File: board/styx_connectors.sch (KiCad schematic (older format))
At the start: 15 parts, among them J3 Conn_01x08, J4 Styx_P4, J5 Styx_P5

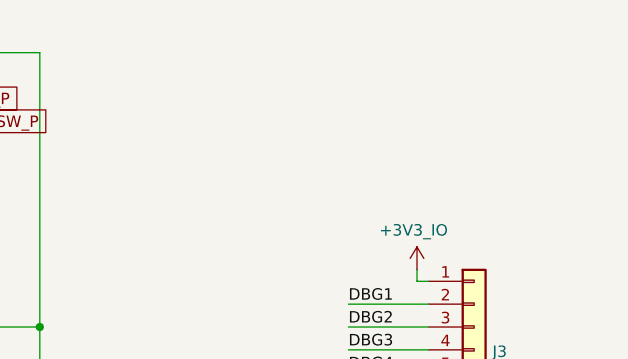
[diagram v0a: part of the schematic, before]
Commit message: Board: initial rearranging to allow for a cover
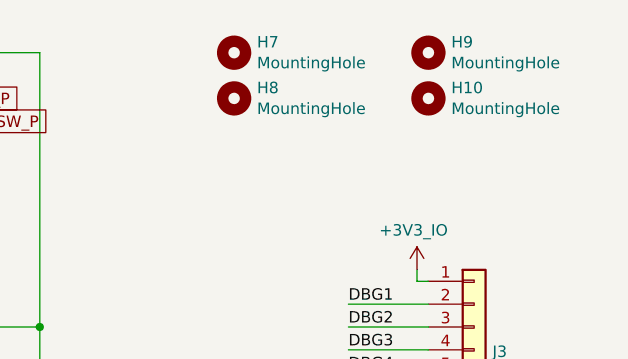
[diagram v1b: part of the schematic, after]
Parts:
- added H10, H7, H8, H9: MountingHole, agc_monitor:MountingHole_ANSI_4, symbol Mechanical:MountingHole
- J3: footprint Connector_PinSocket_2.54mm:PinSocket_2x04_P2.54mm_Vertical -> Connector_PinSocket_2.54mm:PinSocket_2x04_P2.54mm_Horizontal
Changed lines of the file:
@@
 F 0 "J3" H 9830 2142 50  0000 L CNN
 F 1 "Conn_01x08" H 9830 2051 50  0000 L CNN
-F 2 "Connector_PinSocket_2.54mm:PinSocket_2x04_P2.54mm_Vertical" H 9750 2150 50  0001 C CNN
+F 2 "Connector_PinSocket_2.54mm:PinSocket_2x04_P2.54mm_Horizontal" H 9750 2150 50  0001 C CNN
 F 3 "~" H 9750 2150 50  0001 C CNN
 	1    9750 2150
@@
 	4750 6150 4750 6100
 Connection ~ 4750 6100
+$Comp
+L Mechanical:MountingHole H7
+U 1 1 5C9779E4
+P 8700 850
+F 0 "H7" H 8800 896 50  0000 L CNN
+F 1 "MountingHole" H 8800 805 50  0000 L CNN
+F 2 "agc_monitor:MountingHole_ANSI_4" H 8700 850 50  0001 C CNN
+F 3 "~" H 8700 850 50  0001 C CNN
+	1    8700 850
+	1    0    0    -1
+$EndComp
+$Comp
+L Mechanical:MountingHole H8
+U 1 1 5C98D89C
+P 8700 1050
+F 0 "H8" H 8800 1096 50  0000 L CNN
+F 1 "MountingHole" H 8800 1005 50  0000 L CNN
+F 2 "agc_monitor:MountingHole_ANSI_4" H 8700 1050 50  0001 C CNN
+F 3 "~" H 8700 1050 50  0001 C CNN
+	1    8700 1050
+	1    0    0    -1
+$EndComp
+$Comp
+L Mechanical:MountingHole H9
+U 1 1 5C9A3644
+P 9550 850
+F 0 "H9" H 9650 896 50  0000 L CNN
+F 1 "MountingHole" H 9650 805 50  0000 L CNN
+F 2 "agc_monitor:MountingHole_ANSI_4" H 9550 850 50  0001 C CNN
+F 3 "~" H 9550 850 50  0001 C CNN
+	1    9550 850
+	1    0    0    -1
+$EndComp
+$Comp
+L Mechanical:MountingHole H10
+U 1 1 5C9A364A
+P 9550 1050
+F 0 "H10" H 9650 1096 50  0000 L CNN
+F 1 "MountingHole" H 9650 1005 50  0000 L CNN
+F 2 "agc_monitor:MountingHole_ANSI_4" H 9550 1050 50  0001 C CNN
+F 3 "~" H 9550 1050 50  0001 C CNN
+	1    9550 1050
+	1    0    0    -1
+$EndComp
 $EndSCHEMATC

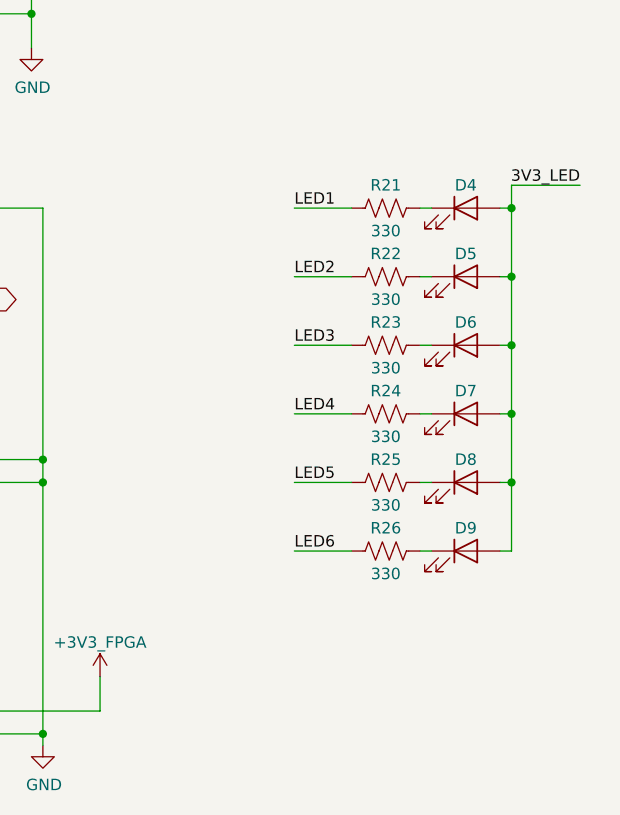
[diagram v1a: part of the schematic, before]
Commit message: Board: more rearranging work on the front; a bit more yet to come
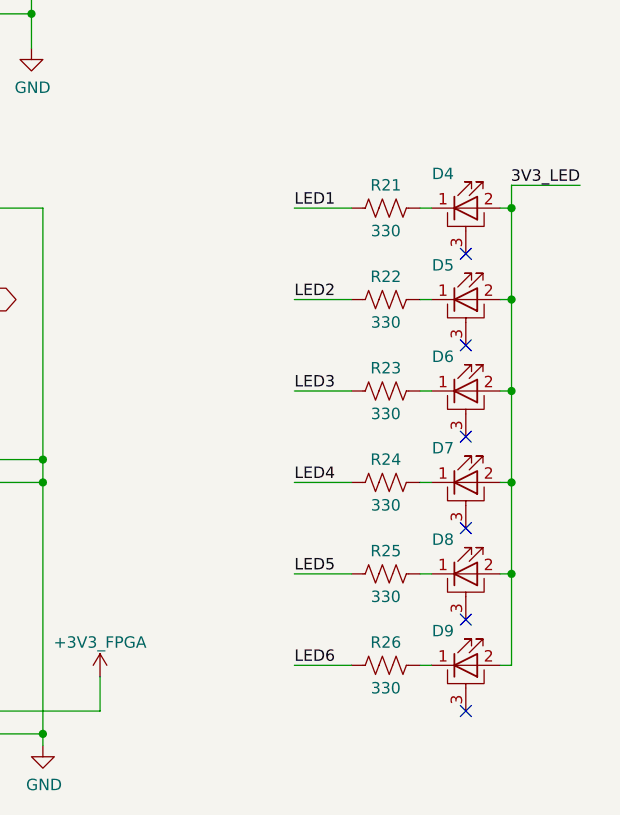
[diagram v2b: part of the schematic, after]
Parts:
- removed D4, D5, D6, D7, D8, D9: LED, LED_SMD:LED_0603_1608Metric, symbol Device:LED
- added D4, D5, D6, D7, D8, D9: LED_PAD, agc_monitor:apa3010, symbol Device:LED_PAD
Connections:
- net 3V3_LED: now also D4.2 (A), D5.2 (A), D6.2 (A), D7.2 (A), D8.2 (A), D9.2 (A)
- net at R25.1: now also D8.1 (K)
- net at R26.1: now also D9.1 (K)
- net at R21.1: now also D4.1 (K)
- net at R22.1: now also D5.1 (K)
- net at R23.1: now also D6.1 (K)
- net at R24.1: now also D7.1 (K)
- no-connect marks 16 -> 22
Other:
- moved on the sheet: R22, R23, R24, R25, R26
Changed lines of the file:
@@
 Text Label 9200 2250 0    50   ~ 0
 DBG4
-$Comp
-L Device:LED D4
-U 1 1 5E9D86D0
-P 9750 3900
-F 0 "D4" H 9750 4000 50  0000 C CNN
-F 1 "LED" H 9741 4025 50  0001 C CNN
-F 2 "LED_SMD:LED_0603_1608Metric" H 9750 3900 50  0001 C CNN
-F 3 "~" H 9750 3900 50  0001 C CNN
-	1    9750 3900
-	1    0    0    -1
-$EndComp
 Wire Wire Line
 	9250 3900 9000 3900
@@
 Wire Wire Line
 	9950 3900 9950 3800
-$Comp
-L Device:LED D5
-U 1 1 5EA444DA
-P 9750 4200
-F 0 "D5" H 9750 4300 50  0000 C CNN
-F 1 "LED" H 9741 4325 50  0001 C CNN
-F 2 "LED_SMD:LED_0603_1608Metric" H 9750 4200 50  0001 C CNN
-F 3 "~" H 9750 4200 50  0001 C CNN
-	1    9750 4200
-	1    0    0    -1
-$EndComp
-Wire Wire Line
-	9250 4200 9000 4200
-Text Label 9000 4200 0    50   ~ 0
+Wire Wire Line
+	9250 4300 9000 4300
+Text Label 9000 4300 0    50   ~ 0
 LED2
 $Comp
 L Device:R_US R22
 U 1 1 5EA444E2
-P 9400 4200
-F 0 "R22" V 9300 4200 50  0000 C CNN
-F 1 "330" V 9500 4200 50  0000 C CNN
-F 2 "Resistor_SMD:R_0603_1608Metric" V 9440 4190 50  0001 C CNN
-F 3 "~" H 9400 4200 50  0001 C CNN
-	1    9400 4200
-	0    1    1    0
-$EndComp
-Wire Wire Line
-	9600 4200 9550 4200
-Wire Wire Line
-	9950 3900 9950 4200
-Wire Wire Line
-	9950 4200 9900 4200
+P 9400 4300
+F 0 "R22" V 9300 4300 50  0000 C CNN
+F 1 "330" V 9500 4300 50  0000 C CNN
+F 2 "Resistor_SMD:R_0603_1608Metric" V 9440 4290 50  0001 C CNN
+F 3 "~" H 9400 4300 50  0001 C CNN
+	1    9400 4300
+	0    1    1    0
+$EndComp
+Wire Wire Line
+	9600 4300 9550 4300
+Wire Wire Line
+	9950 3900 9950 4300
+Wire Wire Line
+	9950 4300 9900 4300
 Connection ~ 9950 3900
-$Comp
-L Device:LED D6
-U 1 1 5EA8C97F
-P 9750 4500
-F 0 "D6" H 9750 4600 50  0000 C CNN
-F 1 "LED" H 9741 4625 50  0001 C CNN
-F 2 "LED_SMD:LED_0603_1608Metric" H 9750 4500 50  0001 C CNN
-F 3 "~" H 9750 4500 50  0001 C CNN
-	1    9750 4500
-	1    0    0    -1
-$EndComp
-Wire Wire Line
-	9250 4500 9000 4500
-Text Label 9000 4500 0    50   ~ 0
+Wire Wire Line
+	9250 4700 9000 4700
+Text Label 9000 4700 0    50   ~ 0
 LED3
 $Comp
 L Device:R_US R23
 U 1 1 5EA8C987
-P 9400 4500
-F 0 "R23" V 9300 4500 50  0000 C CNN
-F 1 "330" V 9500 4500 50  0000 C CNN
-F 2 "Resistor_SMD:R_0603_1608Metric" V 9440 4490 50  0001 C CNN
-F 3 "~" H 9400 4500 50  0001 C CNN
-	1    9400 4500
-	0    1    1    0
-$EndComp
-Wire Wire Line
-	9600 4500 9550 4500
-Wire Wire Line
-	9900 4500 9950 4500
-$Comp
-L Device:LED D7
-U 1 1 5EA8C98F
-P 9750 4800
-F 0 "D7" H 9750 4900 50  0000 C CNN
-F 1 "LED" H 9741 4925 50  0001 C CNN
-F 2 "LED_SMD:LED_0603_1608Metric" H 9750 4800 50  0001 C CNN
-F 3 "~" H 9750 4800 50  0001 C CNN
-	1    9750 4800
-	1    0    0    -1
-$EndComp
-Wire Wire Line
-	9250 4800 9000 4800
-Text Label 9000 4800 0    50   ~ 0
+P 9400 4700
+F 0 "R23" V 9300 4700 50  0000 C CNN
+F 1 "330" V 9500 4700 50  0000 C CNN
+F 2 "Resistor_SMD:R_0603_1608Metric" V 9440 4690 50  0001 C CNN
+F 3 "~" H 9400 4700 50  0001 C CNN
+	1    9400 4700
+	0    1    1    0
+$EndComp
+Wire Wire Line
+	9600 4700 9550 4700
+Wire Wire Line
+	9900 4700 9950 4700
+Wire Wire Line
+	9250 5100 9000 5100
+Text Label 9000 5100 0    50   ~ 0
 LED4
 $Comp
 L Device:R_US R24
 U 1 1 5EA8C997
-P 9400 4800
-F 0 "R24" V 9300 4800 50  0000 C CNN
-F 1 "330" V 9500 4800 50  0000 C CNN
-F 2 "Resistor_SMD:R_0603_1608Metric" V 9440 4790 50  0001 C CNN
-F 3 "~" H 9400 4800 50  0001 C CNN
-	1    9400 4800
-	0    1    1    0
-$EndComp
-Wire Wire Line
-	9600 4800 9550 4800
-Wire Wire Line
-	9950 4800 9900 4800
-Wire Wire Line
-	9950 4500 9950 4200
-Connection ~ 9950 4200
-Wire Wire Line
-	9950 4800 9950 4500
-Connection ~ 9950 4500
+P 9400 5100
+F 0 "R24" V 9300 5100 50  0000 C CNN
+F 1 "330" V 9500 5100 50  0000 C CNN
+F 2 "Resistor_SMD:R_0603_1608Metric" V 9440 5090 50  0001 C CNN
+F 3 "~" H 9400 5100 50  0001 C CNN
+	1    9400 5100
+	0    1    1    0
+$EndComp
+Wire Wire Line
+	9600 5100 9550 5100
+Wire Wire Line
+	9950 5100 9900 5100
+Wire Wire Line
+	9950 4700 9950 4300
+Connection ~ 9950 4300
+Wire Wire Line
+	9950 5100 9950 4700
+Connection ~ 9950 4700
 Wire Wire Line
 	9550 2350 9200 2350
@@
 	1    0    0    -1
 $EndComp
-$Comp
-L Device:LED D8
-U 1 1 5E5887E3
-P 9750 5100
-F 0 "D8" H 9750 5200 50  0000 C CNN
-F 1 "LED" H 9741 5225 50  0001 C CNN
-F 2 "LED_SMD:LED_0603_1608Metric" H 9750 5100 50  0001 C CNN
-F 3 "~" H 9750 5100 50  0001 C CNN
-	1    9750 5100
-	1    0    0    -1
-$EndComp
-Wire Wire Line
-	9250 5100 9000 5100
-Text Label 9000 5100 0    50   ~ 0
+Wire Wire Line
+	9250 5500 9000 5500
+Text Label 9000 5500 0    50   ~ 0
 LED5
 $Comp
 L Device:R_US R25
 U 1 1 5E5887EB
-P 9400 5100
-F 0 "R25" V 9300 5100 50  0000 C CNN
-F 1 "330" V 9500 5100 50  0000 C CNN
-F 2 "Resistor_SMD:R_0603_1608Metric" V 9440 5090 50  0001 C CNN
-F 3 "~" H 9400 5100 50  0001 C CNN
-	1    9400 5100
-	0    1    1    0
-$EndComp
-Wire Wire Line
-	9600 5100 9550 5100
-Wire Wire Line
-	9950 5100 9900 5100
-Wire Wire Line
-	9950 4800 9950 5100
-Connection ~ 9950 4800
-$Comp
-L Device:LED D9
-U 1 1 5E5B5AA7
-P 9750 5400
-F 0 "D9" H 9750 5500 50  0000 C CNN
-F 1 "LED" H 9741 5525 50  0001 C CNN
-F 2 "LED_SMD:LED_0603_1608Metric" H 9750 5400 50  0001 C CNN
-F 3 "~" H 9750 5400 50  0001 C CNN
-	1    9750 5400
-	1    0    0    -1
-$EndComp
-Wire Wire Line
-	9250 5400 9000 5400
-Text Label 9000 5400 0    50   ~ 0
+P 9400 5500
+F 0 "R25" V 9300 5500 50  0000 C CNN
+F 1 "330" V 9500 5500 50  0000 C CNN
+F 2 "Resistor_SMD:R_0603_1608Metric" V 9440 5490 50  0001 C CNN
+F 3 "~" H 9400 5500 50  0001 C CNN
+	1    9400 5500
+	0    1    1    0
+$EndComp
+Wire Wire Line
+	9600 5500 9550 5500
+Wire Wire Line
+	9950 5500 9900 5500
+Wire Wire Line
+	9950 5100 9950 5500
+Connection ~ 9950 5100
+Wire Wire Line
+	9250 5900 9000 5900
+Text Label 9000 5900 0    50   ~ 0
 LED6
 $Comp
 L Device:R_US R26
 U 1 1 5E5B5AAF
-P 9400 5400
-F 0 "R26" V 9300 5400 50  0000 C CNN
-F 1 "330" V 9500 5400 50  0000 C CNN
-F 2 "Resistor_SMD:R_0603_1608Metric" V 9440 5390 50  0001 C CNN
-F 3 "~" H 9400 5400 50  0001 C CNN
-	1    9400 5400
-	0    1    1    0
-$EndComp
-Wire Wire Line
-	9600 5400 9550 5400
-Wire Wire Line
-	9950 5400 9900 5400
-Wire Wire Line
-	9950 5100 9950 5400
-Connection ~ 9950 5100
+P 9400 5900
+F 0 "R26" V 9300 5900 50  0000 C CNN
+F 1 "330" V 9500 5900 50  0000 C CNN
+F 2 "Resistor_SMD:R_0603_1608Metric" V 9440 5890 50  0001 C CNN
+F 3 "~" H 9400 5900 50  0001 C CNN
+	1    9400 5900
+	0    1    1    0
+$EndComp
+Wire Wire Line
+	9600 5900 9550 5900
+Wire Wire Line
+	9950 5900 9900 5900
+Wire Wire Line
+	9950 5500 9950 5900
+Connection ~ 9950 5500
 Connection ~ 5550 1250
 Wire Wire Line
@@
 	1    0    0    -1
 $EndComp
+$Comp
+L Device:LED_PAD D4
+U 1 1 5CB34036
+P 9750 3900
+F 0 "D4" H 9650 4050 50  0000 C CNN
+F 1 "LED_PAD" H 9750 4089 50  0001 C CNN
+F 2 "agc_monitor:apa3010" H 9750 3900 50  0001 C CNN
+F 3 "~" H 9750 3900 50  0001 C CNN
+	1    9750 3900
+	1    0    0    -1
+$EndComp
+NoConn ~ 9750 4100
+$Comp
+L Device:LED_PAD D5
+U 1 1 5CBCE514
+P 9750 4300
+F 0 "D5" H 9650 4450 50  0000 C CNN
+F 1 "LED_PAD" H 9750 4489 50  0001 C CNN
+F 2 "agc_monitor:apa3010" H 9750 4300 50  0001 C CNN
+F 3 "~" H 9750 4300 50  0001 C CNN
+	1    9750 4300
+	1    0    0    -1
+$EndComp
+NoConn ~ 9750 4500
+$Comp
+L Device:LED_PAD D6
+U 1 1 5CBE4210
+P 9750 4700
+F 0 "D6" H 9650 4850 50  0000 C CNN
+F 1 "LED_PAD" H 9750 4889 50  0001 C CNN
+F 2 "agc_monitor:apa3010" H 9750 4700 50  0001 C CNN
+F 3 "~" H 9750 4700 50  0001 C CNN
+	1    9750 4700
+	1    0    0    -1
+$EndComp
+NoConn ~ 9750 4900
+$Comp
+L Device:LED_PAD D7
+U 1 1 5CBF9F4C
+P 9750 5100
+F 0 "D7" H 9650 5250 50  0000 C CNN
+F 1 "LED_PAD" H 9750 5289 50  0001 C CNN
+F 2 "agc_monitor:apa3010" H 9750 5100 50  0001 C CNN
+F 3 "~" H 9750 5100 50  0001 C CNN
+	1    9750 5100
+	1    0    0    -1
+$EndComp
+NoConn ~ 9750 5300
+$Comp
+L Device:LED_PAD D8
+U 1 1 5CBF9F53
+P 9750 5500
+F 0 "D8" H 9650 5650 50  0000 C CNN
+F 1 "LED_PAD" H 9750 5689 50  0001 C CNN
+F 2 "agc_monitor:apa3010" H 9750 5500 50  0001 C CNN
+F 3 "~" H 9750 5500 50  0001 C CNN
+	1    9750 5500
+	1    0    0    -1
+$EndComp
+NoConn ~ 9750 5700
+$Comp
+L Device:LED_PAD D9
+U 1 1 5CC0FC57
+P 9750 5900
+F 0 "D9" H 9650 6050 50  0000 C CNN
+F 1 "LED_PAD" H 9750 6089 50  0001 C CNN
+F 2 "agc_monitor:apa3010" H 9750 5900 50  0001 C CNN
+F 3 "~" H 9750 5900 50  0001 C CNN
+	1    9750 5900
+	1    0    0    -1
+$EndComp
+NoConn ~ 9750 6100
 $EndSCHEMATC
